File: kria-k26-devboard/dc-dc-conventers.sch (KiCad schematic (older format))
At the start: 71 parts, among them U10 AP62301WU-7, U11 AP62301WU-7, U2 AP62301WU-7, U4 AP62301WU-7, U5 AP62301WU-7, U6 AP62301WU-7, U7 AP62301WU-7, U8 RPX-4.0-R, U9 AP62301WU-7

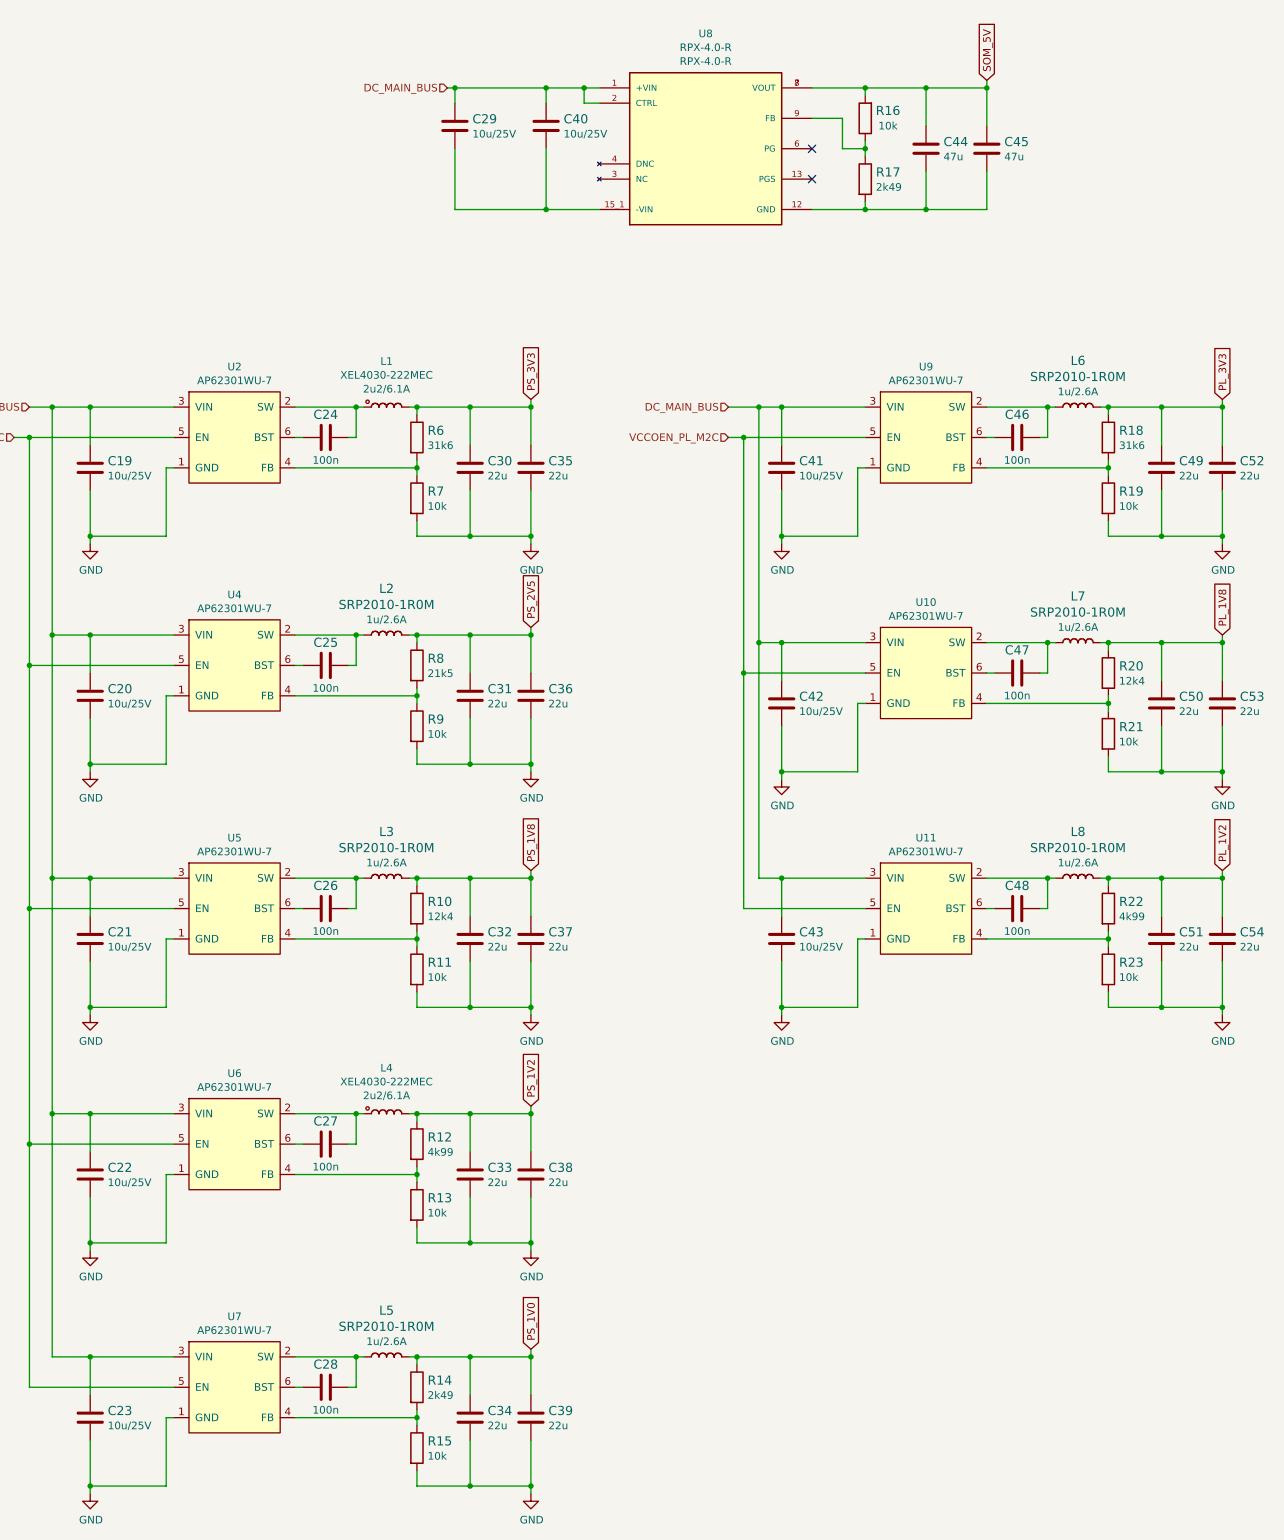
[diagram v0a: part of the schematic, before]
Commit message: Finished reset logic, added crystal gen. to USB PHY, create power toggle for SD 3.0
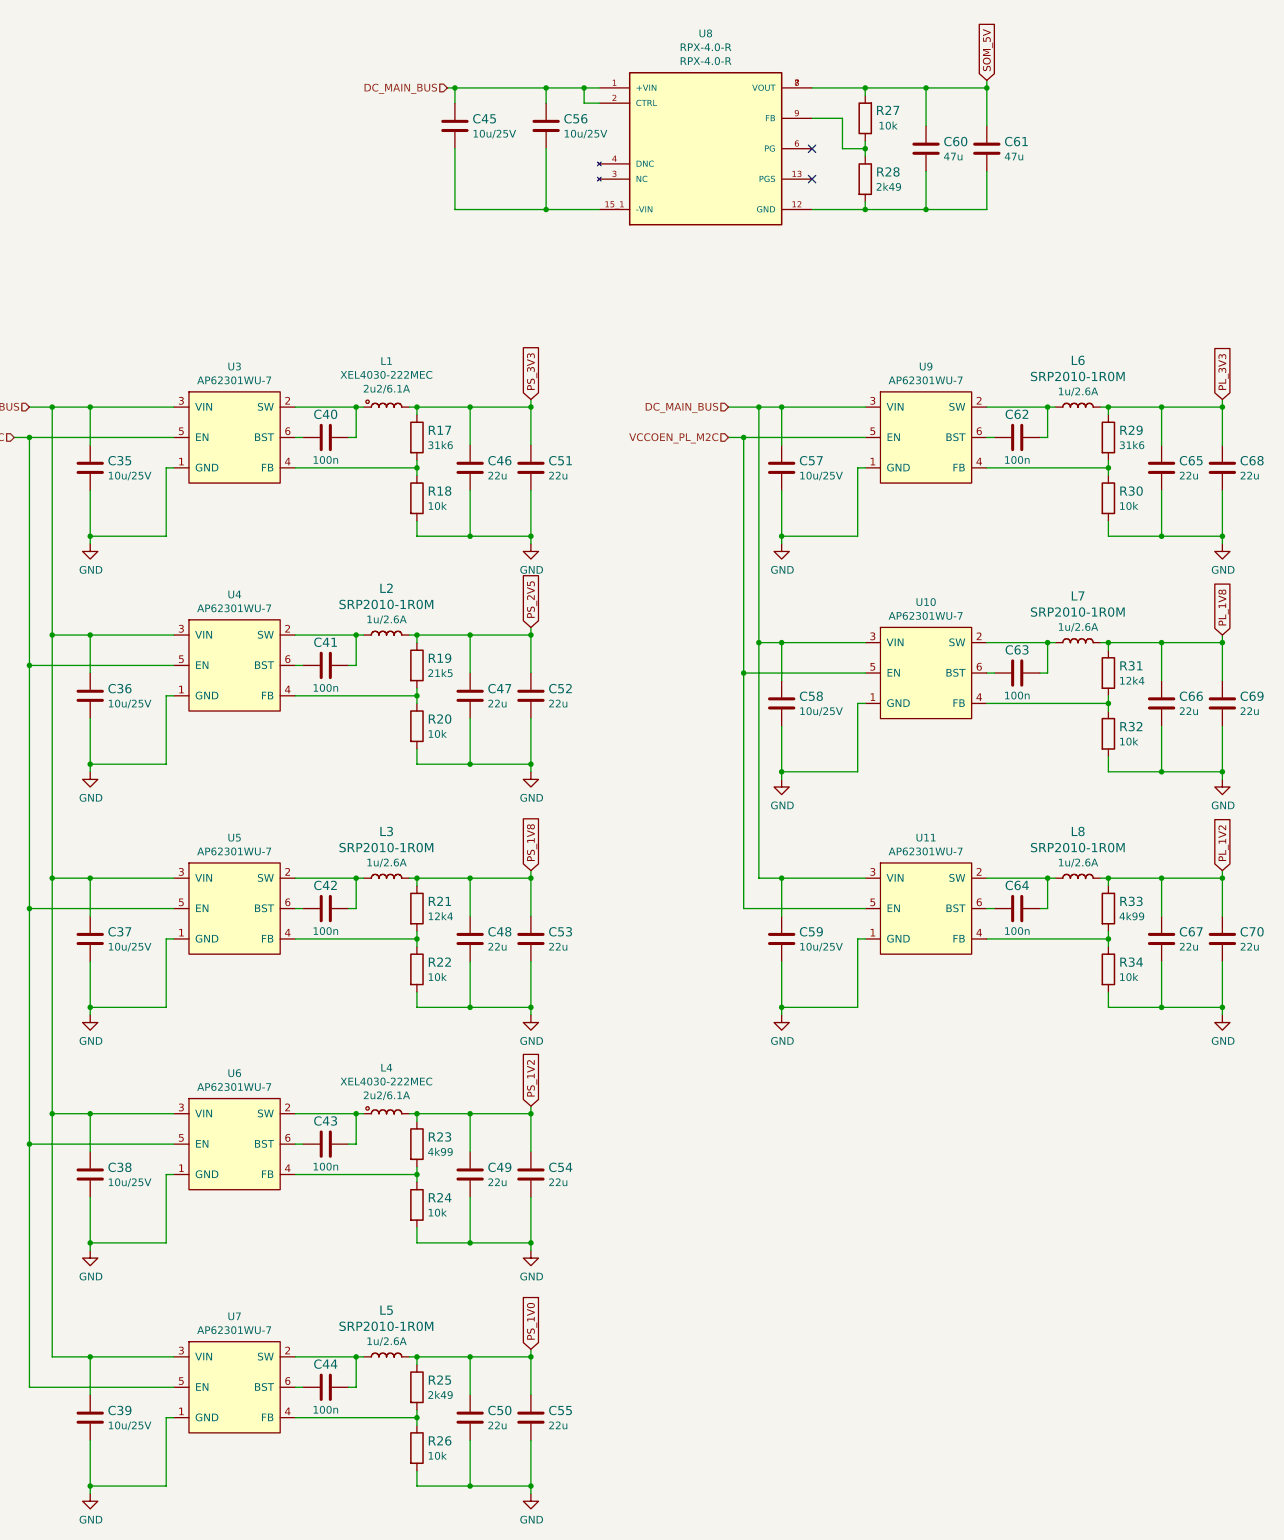
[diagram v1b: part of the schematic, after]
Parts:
- renumbered C19 to C35, C20 to C36, C21 to C37, C22 to C38, C23 to C39, C24 to C40, C25 to C41, C26 to C42, C27 to C43, C28 to C44, C29 to C45, C30 to C46, C31 to C47, C32 to C48, C33 to C49, C34 to C50, C35 to C51, C36 to C52, C37 to C53, C38 to C54, C39 to C55, C40 to C56, C41 to C57, C42 to C58, C43 to C59, C44 to C60, C45 to C61, C46 to C62, C47 to C63, C48 to C64, C49 to C65, C50 to C66, C51 to C67, C52 to C68, C53 to C69, C54 to C70, R6 to R17, R7 to R18, R8 to R19, R9 to R20, R10 to R21, R11 to R22, R12 to R23, R13 to R24, R14 to R25, R15 to R26, R16 to R27, R17 to R28, R18 to R29, R19 to R30, R20 to R31, R21 to R32, R22 to R33, R23 to R34, U2 to U3

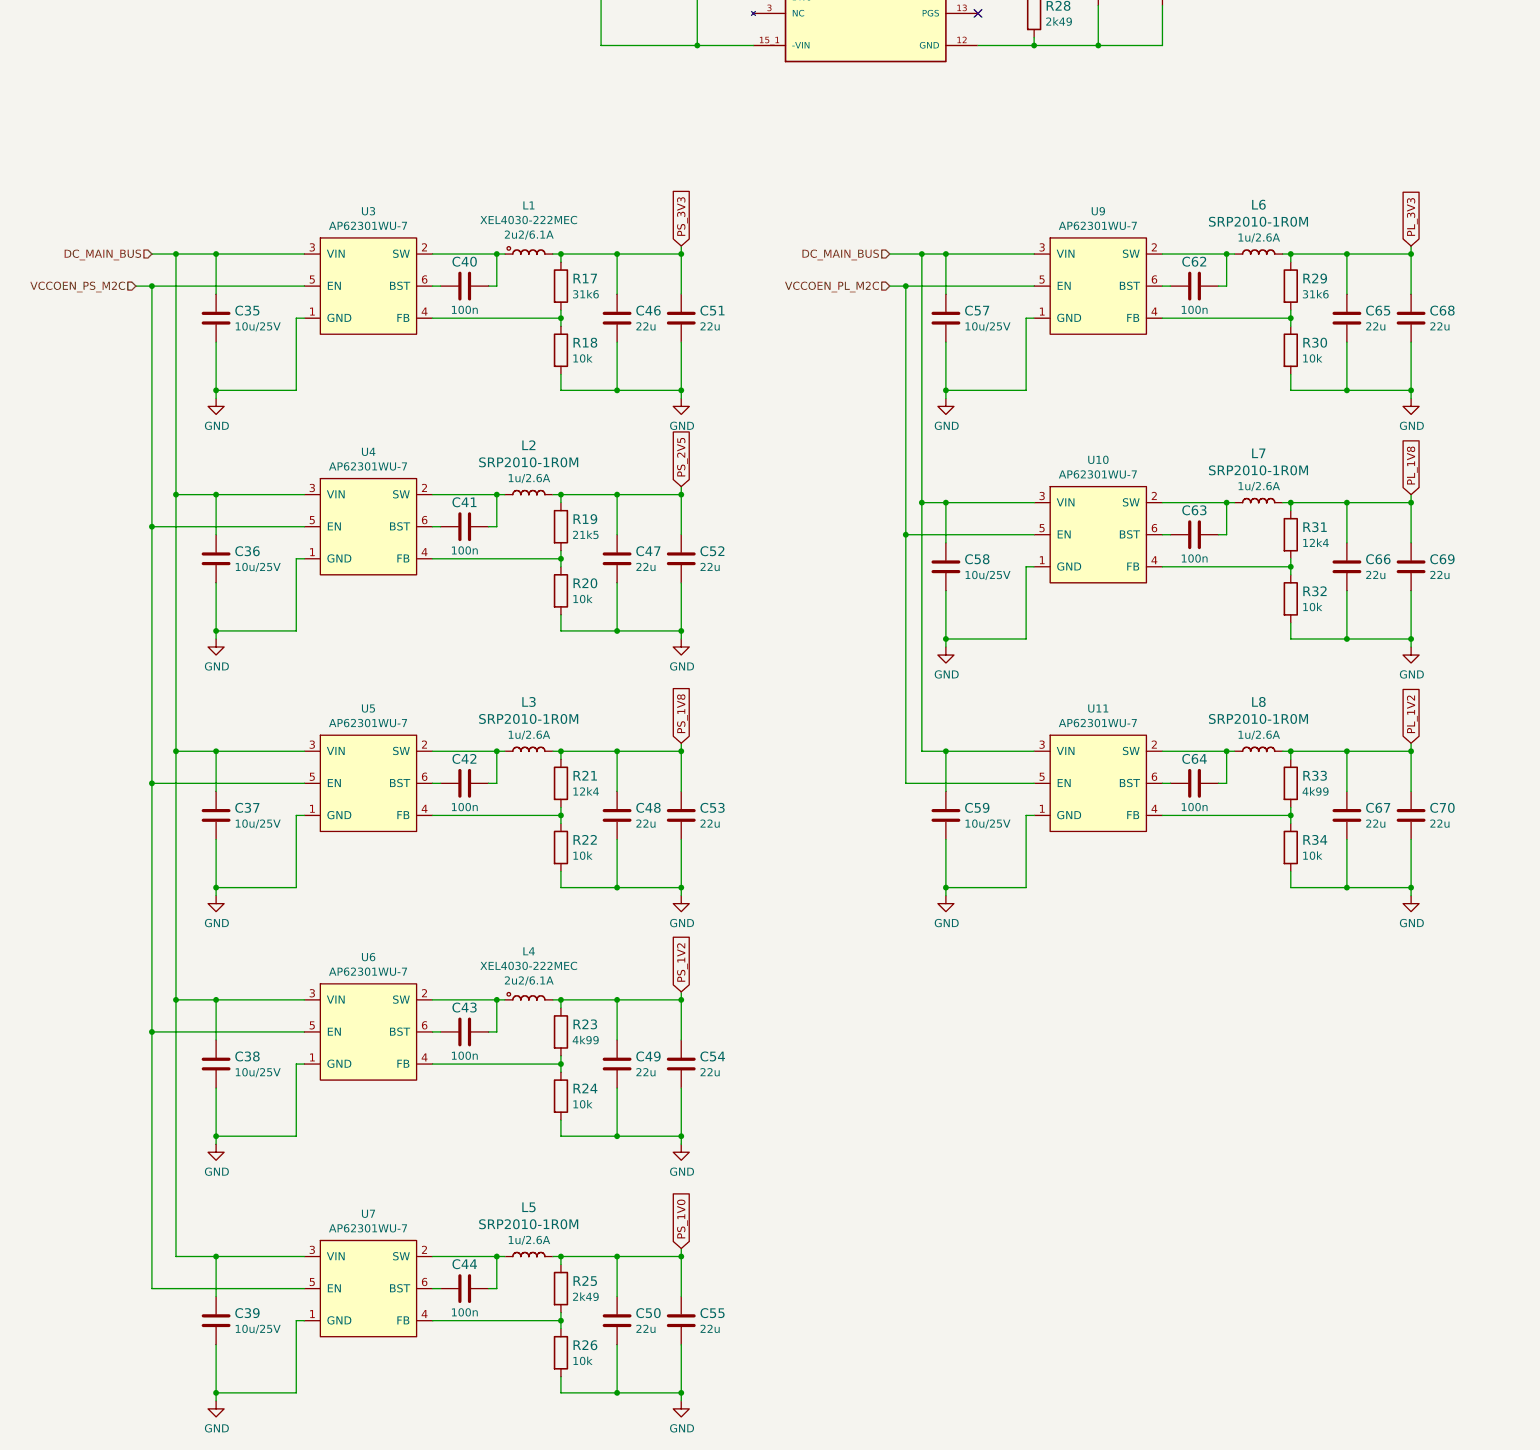
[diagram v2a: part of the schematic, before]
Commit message: Fixes on Reset pagae, progress through clock sheet
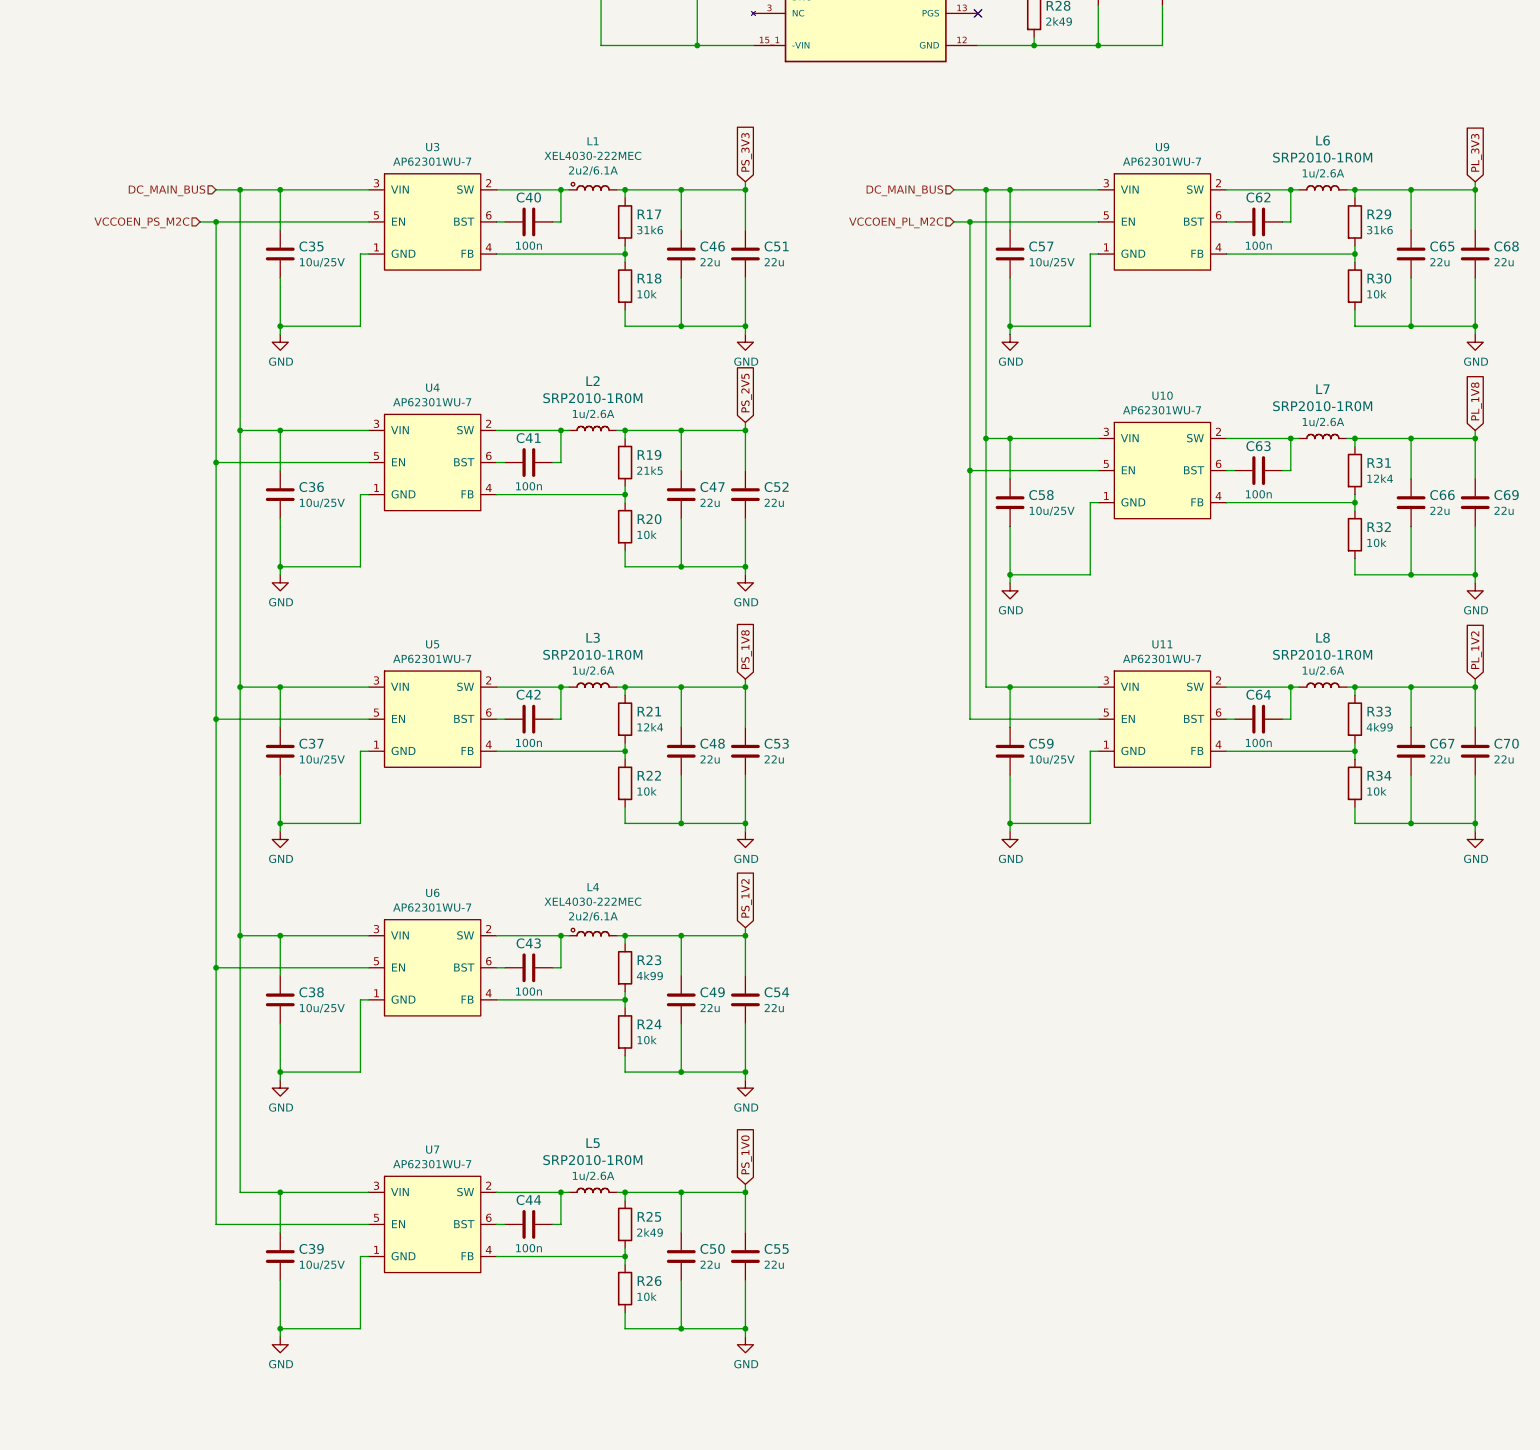
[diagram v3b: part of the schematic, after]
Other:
- moved on the sheet: C35, C36, C37, C38, C39, C40, C41, C42, C43, C44, C46, C47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

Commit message: Added Led voltage indicator, fan circuit. Tidied up supply and SOM sheet
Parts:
- added D? (x6): LG_L29K-G2J1-24-Z, antmicro-footprints:LED_0603, symbol antmicroLEDIndicationDiscrete:LG_L29K-G2J1-24-Z
- added Q? (x3): BC847, antmicro-footprints:SOT-23-3, symbol antmicroTransistorsBipolarSingle:BC847
- added R?: R_2k_0402, antmicro-footprints:0402-res, symbol antmicroResistors0402:R_2k_0402
- added R? (x5): R_1k_0402, antmicro-footprints:0402-res, symbol antmicroResistors0402:R_1k_0402
- added R?: R_510R_0402, antmicro-footprints:0402-res, symbol antmicroResistors0402:R_510R_0402
- added R? (x2): R_68_0402, antmicro-footprints:0402-res, symbol antmicroResistors0402:R_68_0402
- added R? (x3): R_10k_0402, antmicro-footprints:0402-res, symbol antmicroResistors0402:R_10k_0402
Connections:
- net GND: now also D?.2, D?.2, D?.2, D?.2, D?.2, D?.2, Q?.2 (E), Q?.2 (E), Q?.2 (E)
- net PL_1V2: now also R?.1
- net PL_1V8: now also R?.1
- net PL_3V3: now also R?.1, R?.1
- net PS_1V0: now also R?.1
- net PS_1V2: now also R?.1
- net PS_1V8: now also R?.1
- net PS_2V5: now also R?.2
- net PS_3V3: now also R?.1, R?.1, R?.1
- net SOM_5V: now also R?.2
- new net: D?.1, R?.1 (x2)
- new net: D?.1, R?.2 (x4)
- new net: Q?.3 (C), R?.2 (x3)
- new net: Q?.1 (B), R?.2 (x3)
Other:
- note added: "PL domain"
- note added: "PS domain"
- note added: "Power indication"
- note added: "SOM 5V"
- moved on the sheet: C35, C36, C37, C38, C39, C40, C41, C42, C43, C44, C45, C46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
